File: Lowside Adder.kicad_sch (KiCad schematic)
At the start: 10 parts, among them U10 VNL5090, U11 VNL5090, U12 VNL5090, U9 VNL5090

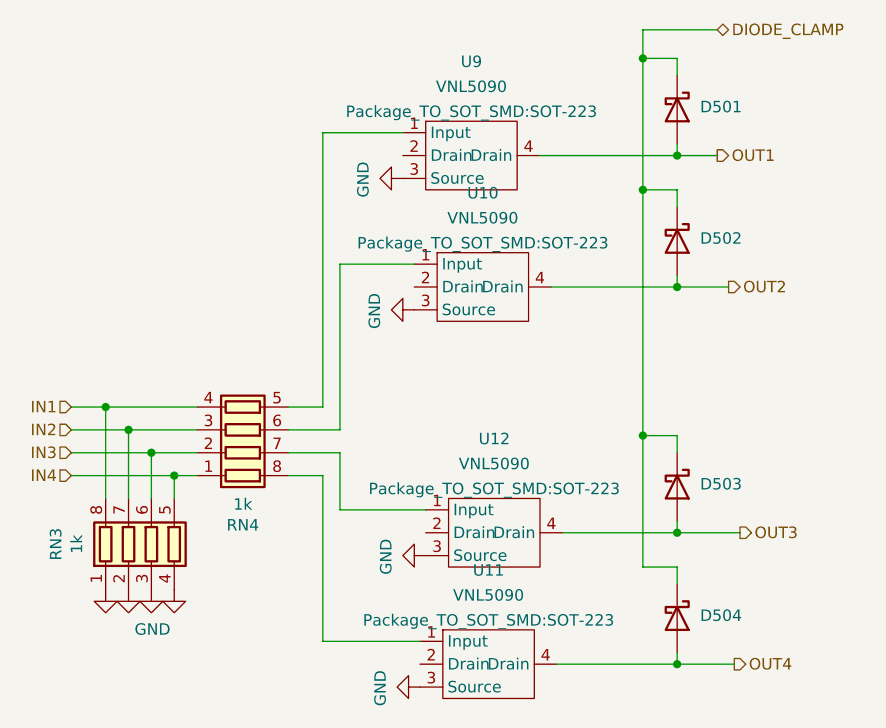
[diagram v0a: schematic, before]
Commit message: Changes to discrete VR
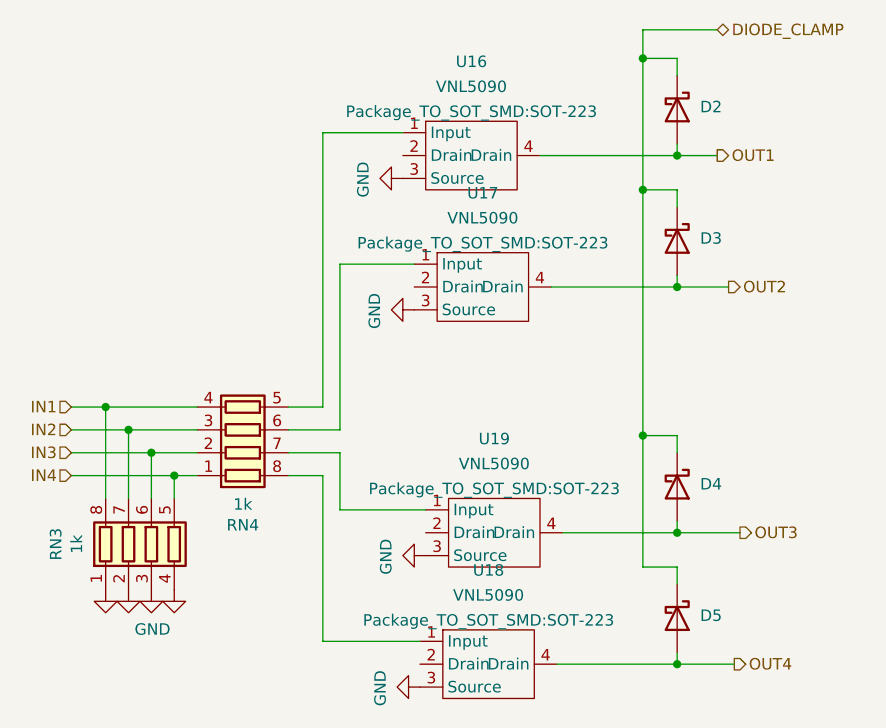
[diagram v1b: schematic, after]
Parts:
- renumbered D501 to D2, D502 to D3, D503 to D4, D504 to D5, U9 to U16, U10 to U17, U11 to U18, U12 to U19

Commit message: V1.0 published
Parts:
- renumbered D2 to D6, D3 to D7, D4 to D8, D5 to D9
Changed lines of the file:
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@@
 		(dnp no)
 		(fields_autoplaced yes)
-		(property "Reference" "D3"
+		(property "Reference" "D7"
 			(at 160.02 62.5475 90)
 			(effects
@@
 		(dnp no)
 		(fields_autoplaced yes)
-		(property "Reference" "D5"
+		(property "Reference" "D9"
 			(at 160.02 104.4575 90)
 			(effects
@@
 		(dnp no)
 		(fields_autoplaced yes)
-		(property "Reference" "D4"
+		(property "Reference" "D8"
 			(at 160.02 89.8525 90)
 			(effects
@@
 		(dnp no)
 		(fields_autoplaced yes)
-		(property "Reference" "D2"
+		(property "Reference" "D6"
 			(at 160.02 47.9425 90)
 			(effects

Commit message: Fixed trigger scope
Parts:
- renumbered D6 to D2, D7 to D3, D8 to D4, D9 to D5, RN3 to RN1, RN4 to RN2, U16 to U11, U17 to U12, U18 to U13, U19 to U14
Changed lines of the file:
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@@
 (kicad_sch
-	(version 20231120)
+	(version 20250114)
 	(generator "eeschema")
-	(generator_version "8.0")
+	(generator_version "9.0")
 	(paper "A4")
 	(title_block
@@
 		(shape output)
 		(at 163.83 109.855 0)
-		(fields_autoplaced yes)
 		(effects
 			(font
@@
 		(shape input)
 		(at 90.17 83.82 180)
-		(fields_autoplaced yes)
 		(effects
 			(font
@@
 		(shape input)
 		(at 90.17 88.9 180)
-		(fields_autoplaced yes)
 		(effects
 			(font
@@
 		(shape output)
 		(at 164.465 95.25 0)
-		(fields_autoplaced yes)
 		(effects
 			(font
@@
 		(shape input)
 		(at 90.17 86.36 180)
-		(fields_autoplaced yes)
 		(effects
 			(font
@@
 		(shape input)
 		(at 90.17 81.28 180)
-		(fields_autoplaced yes)
 		(effects
 			(font
@@
 		(shape bidirectional)
 		(at 161.925 39.37 0)
-		(fields_autoplaced yes)
 		(effects
 			(font
@@
 		(shape output)
 		(at 163.195 67.945 0)
-		(fields_autoplaced yes)
 		(effects
 			(font
@@
 		(shape output)
 		(at 161.925 53.34 0)
-		(fields_autoplaced yes)
 		(effects
 			(font
@@
 		(dnp no)
 		(fields_autoplaced yes)
-		(property "Reference" "U17"
+		(property "Reference" "U12"
 			(at 135.89 57.5203 0)
 			(effects
@@
 		(on_board yes)
 		(dnp no)
-		(property "Reference" "#PWR0136"
+		(property "Reference" "#PWR0121"
 			(at 120.65 55.88 0)
 			(effects
@@
 		(dnp no)
 		(fields_autoplaced yes)
-		(property "Reference" "U19"
+		(property "Reference" "U14"
 			(at 137.16 84.8253 0)
 			(effects
@@
 		(on_board yes)
 		(dnp no)
-		(property "Reference" "#PWR0132"
+		(property "Reference" "#PWR0117"
 			(at 93.98 107.95 0)
 			(effects
@@
 		(on_board yes)
 		(dnp no)
-		(property "Reference" "#PWR0139"
+		(property "Reference" "#PWR0124"
 			(at 123.19 97.79 0)
 			(effects
@@
 		(on_board yes)
 		(dnp no)
-		(property "Reference" "#PWR0133"
+		(property "Reference" "#PWR0118"
 			(at 96.52 107.95 0)
 			(effects
@@
 		(dnp no)
 		(fields_autoplaced yes)
-		(property "Reference" "D7"
+		(property "Reference" "D3"
 			(at 160.02 62.5475 90)
 			(effects
@@
 		(on_board yes)
 		(dnp no)
-		(property "Reference" "#PWR0135"
+		(property "Reference" "#PWR0120"
 			(at 101.6 107.95 0)
 			(effects
@@
 		(dnp no)
 		(fields_autoplaced yes)
-		(property "Reference" "D9"
+		(property "Reference" "D5"
 			(at 160.02 104.4575 90)
 			(effects
@@
 		(dnp no)
 		(fields_autoplaced yes)
-		(property "Reference" "D8"
+		(property "Reference" "D4"
 			(at 160.02 89.8525 90)
 			(effects
@@
 		(on_board yes)
 		(dnp no)
-		(property "Reference" "#PWR0138"
+		(property "Reference" "#PWR0123"
 			(at 122.555 112.395 0)
 			(effects
@@
 		(on_board yes)
 		(dnp no)
-		(property "Reference" "#PWR0134"
+		(property "Reference" "#PWR0119"
 			(at 99.06 107.95 0)
 			(effects
@@
 		(on_board yes)
 		(dnp no)
-		(property "Reference" "#PWR0137"
+		(property "Reference" "#PWR0122"
 			(at 121.92 70.485 0)
 			(effects
@@
 		(on_board yes)
 		(dnp no)
-		(property "Reference" "RN4"
+		(property "Reference" "RN2"
 			(at 109.22 94.4118 90)
 			(effects
@@
 		(dnp no)
 		(fields_autoplaced yes)
-		(property "Reference" "U16"
+		(property "Reference" "U11"
 			(at 134.62 42.9153 0)
 			(effects
@@
 		(dnp no)
 		(fields_autoplaced yes)
-		(property "Reference" "D6"
+		(property "Reference" "D2"
 			(at 160.02 47.9425 90)
 			(effects
@@
 		(dnp no)
 		(fields_autoplaced yes)
-		(property "Reference" "U18"
+		(property "Reference" "U13"
 			(at 136.525 99.4303 0)
 			(effects
@@
 		(on_board yes)
 		(dnp no)
-		(property "Reference" "RN3"
+		(property "Reference" "RN1"
 			(at 88.4682 96.52 90)
 			(effects
